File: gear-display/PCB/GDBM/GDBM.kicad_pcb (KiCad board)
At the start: 2 copper layers, 7 parts

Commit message: rikki
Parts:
- added ART1: Artwork_DC_Plug_Polarity, KD_Mechanical:ART_DC_POLARITY, F.Cu at (167.4, 131.6)
- added C1: C_1206_10u_50V, KD_Capacitor:C_1206_3216Metric, B.Cu at (150.5, 130.5)
- added C10: C_0603_33p_NP0_5%_100V, KD_Capacitor:C_0603_1608Metric, B.Cu at (134.9, 119.5)
- added C11: C_0805_1u_X7R_25V, KD_Capacitor:C_0805_2012Metric, B.Cu at (139.1, 108.7)
- added C12: C_1206_10u_50V, KD_Capacitor:C_1206_3216Metric, B.Cu at (158.0, 93.5)
- added C13: C_0603_100n_X7R_100V, KD_Capacitor:C_0603_1608Metric, B.Cu at (156.0, 94.2)
- added C14: C_0603_100n_X7R_100V, KD_Capacitor:C_0603_1608Metric, B.Cu at (104.0, 145.5)
- added C15: C_0805_DNP, KD_Capacitor:C_0805_2012Metric_DNP, B.Cu at (107.5, 145.5)
- added C16: C_1206_10u_50V, KD_Capacitor:C_1206_3216Metric, B.Cu at (95.7, 99.0)
- added C17: C_1206_10u_50V, KD_Capacitor:C_1206_3216Metric, B.Cu at (93.3, 99.0)
- added C18: C_1206_10u_50V, KD_Capacitor:C_1206_3216Metric, B.Cu at (95.7, 94.3)
- added C19: C_0603_100n_X7R_100V, KD_Capacitor:C_0603_1608Metric, B.Cu at (107.4, 122.8)
- added C2: C_1206_10u_50V, KD_Capacitor:C_1206_3216Metric, B.Cu at (154.0, 145.5)
- added C20: C_0805_DNP, KD_Capacitor:C_0805_2012Metric_DNP, B.Cu at (110.0, 123.0)
- added C21: C_0805_1u_X7R_25V, KD_Capacitor:C_0805_2012Metric, B.Cu at (130.6, 95.5)
- added C3: C_1206_10u_50V, KD_Capacitor:C_1206_3216Metric, B.Cu at (148.0, 130.5)
- added C4: C_0603_100n_X7R_100V, KD_Capacitor:C_0603_1608Metric, B.Cu at (156.5, 146.0)
- added C5: C_0603_100n_X7R_100V, KD_Capacitor:C_0603_1608Metric, B.Cu at (145.5, 131.2)
- added C6: C_0603_100n_X7R_100V, KD_Capacitor:C_0603_1608Metric, B.Cu at (116.0, 112.0)
- added C7: C_0805_1u_X7R_25V, KD_Capacitor:C_0805_2012Metric, B.Cu at (118.0, 112.0)
- added C8: C_0603_33p_NP0_5%_100V, KD_Capacitor:C_0603_1608Metric, B.Cu at (126.7, 119.5)
- added C9: C_0805_1u_X7R_25V, KD_Capacitor:C_0805_2012Metric, B.Cu at (132.5, 98.0)
- added D1: Schottky_30V_1A_Toshiba_CUS10S30, KD_Diode:D_SOD-323, B.Cu at (157.0, 137.5)
- added D2: TVS_12V_LF_SMAJ12CA, KD_Diode:DIOC530X280X230_SMA_A, B.Cu at (160.0, 141.5)
- added D3: 0603_Green_Clear_LTST-C190KGKT, KD_Diode:LED_0603_1608Metric_Pad1.05x0.95mm_HandSolder, B.Cu at (116.0, 122.1)
- added D4: TVS_5V5_DRTR5V0U4S-7-M, KD_Package_TO_SOT_SMD:SOT-363_SC-70-6, B.Cu at (157.0, 98.7)
- added D5: 7seg_70mm_CA_Lumex_LDS-AD16RI, KD_Display:7seg_70mm_Kingbright_SC23-11SURKWA, F.Cu at (121.0, 113.0)
- added F1: Fuse_1A_C1F_1, KD_Resistor:RESC3216X70N, B.Cu at (162.5, 137.5)
- added FB1: Ferrite_250mA_Murata_BLM15HG102SN1D, KD_Inductor:INDC1005X55N, B.Cu at (161.0, 98.7)
- added H3: NPTH_3.2_M3_Clearance, KD_Mechanical_Mounting_Hole:NPTH_3.2mm_M3_clearance, F.Cu at (87.0, 74.0)
- added H4: NPTH_3.2_M3_Clearance, KD_Mechanical_Mounting_Hole:NPTH_3.2mm_M3_clearance, F.Cu at (175.0, 153.0)
- added H5: NPTH_3.2_M3_Clearance, KD_Mechanical_Mounting_Hole:NPTH_3.2mm_M3_clearance, F.Cu at (175.0, 74.0)
- added H6: NPTH_3.2_M3_Clearance, KD_Mechanical_Mounting_Hole:NPTH_3.2mm_M3_clearance, F.Cu at (155.0, 119.0)
- added J1: Con_Screw_1x04_691313510004, KD_Connector_Screw:CON_508_1X04_691313510004_Mated, F.Cu at (88.0, 113.5)
- added J2: Con_Screw_1x04_691313510004, KD_Connector_Screw:CON_508_1X04_691313510004_Mated, F.Cu at (174.0, 90.0)
- added J3: DC_2.5_5.5_PJ-090BH, KD_Connector_Circular:CON_DC_2.5_5.5_PJ-090BH, B.Cu at (159.8, 128.0)
- added J4: Con_Screw_1x04_691313510004, KD_Connector_Screw:CON_508_1X04_691313510004_Mated, F.Cu at (88.0, 90.0)
- added J5: Con_Screw_1x04_691313510004, KD_Connector_Screw:CON_508_1X04_691313510004_Mated, F.Cu at (174.0, 113.5)
- added J6: Con_Screw_1x04_691313510004, KD_Connector_Screw:CON_508_1X04_691313510004_Mated, F.Cu at (88.0, 137.0)
- added J7: Con_Screw_1x04_691313510004, KD_Connector_Screw:CON_508_1X04_691313510004_Mated, F.Cu at (174.0, 137.0)
- added J8: USB_B_V_Adam_USB-B-S-VT, KD_Connector_USB_HDMI_Etc:USB_B_Vertical_Adam_USB-B-S-VT, B.Cu at (162.0, 106.0)
- added M1: Knob_6mm_BL_RED_CLIFF_CL170842CR, KD_Mechanical:Knob_CLIFF_CL170842CR, F.Cu at (160.5, 81.5)
- added Q1: PMOS_30V_4A1_SIL3407-TP, KD_Package_TO_SOT_SMD:SOT95P280X120-6RN, B.Cu at (110.0, 141.0)
- added R1: R_0805_DNP, KD_Resistor:RESC2012X60N_DNP, B.Cu at (130.9, 118.5)
- added R10: R_0603_10_5%, KD_Resistor:RESC1608X55N, B.Cu at (152.8, 97.7)
- added R11: R_1206_191_1%, KD_Resistor:RESC3216X70N, B.Cu at (122.5, 89.5)
- added R12: R_1206_191_1%, KD_Resistor:RESC3216X70N, B.Cu at (124.5, 137.5)
- added R13: R_1206_191_1%, KD_Resistor:RESC3216X70N, B.Cu at (116.5, 137.5)
- added R14: R_1206_191_1%, KD_Resistor:RESC3216X70N, B.Cu at (110.5, 89.5)
- added R15: R_0603_22k_1%, KD_Resistor:RESC1608X55N, B.Cu at (99.0, 141.0)
- added R16: R_1206_191_1%, KD_Resistor:RESC3216X70N, B.Cu at (126.5, 89.5)
- added R17: R_1206_191_1%, KD_Resistor:RESC3216X70N, B.Cu at (120.5, 137.5)
- added R18: R_1206_191_1%, KD_Resistor:RESC3216X70N, B.Cu at (114.5, 89.5)
- added R19: R_1206_191_1%, KD_Resistor:RESC3216X70N, B.Cu at (118.5, 89.5)
- added R2: R_0603_22k_1%, KD_Resistor:RESC1608X55N, B.Cu at (135.9, 115.0)
- added R20: R_0805_DNP, KD_Resistor:RESC2012X60N_DNP, B.Cu at (99.0, 93.5)
- added R21: R_0805_0_automotive, KD_Resistor:RESC2012X60N, B.Cu at (92.0, 91.6)
- added R22: R_0805_0_automotive, KD_Resistor:RESC2012X60N, B.Cu at (99.0, 95.5)
- added R23: R_0805_0_automotive, KD_Resistor:RESC2012X60N, B.Cu at (162.9, 121.0)
- added R24: R_0805_0_automotive, KD_Resistor:RESC2012X60N, B.Cu at (162.9, 119.0)
- added R25: R_0805_0_automotive, KD_Resistor:RESC2012X60N, B.Cu at (162.9, 117.0)
- added R26: R_0603_22k_1%, KD_Resistor:RESC1608X55N, B.Cu at (102.0, 123.5)
- added R27: R_0603_22k_1%, KD_Resistor:RESC1608X55N, B.Cu at (100.0, 123.5)
- added R28: Pot_V_10k_CUI_PT01-D120K2-B103, KD_Resistor:Potentiometer_CUI_PT01-DX20K2-XXXX, F.Cu at (160.5, 88.8)
- added R29: R_0402_4700_1%, KD_Resistor:RESC1005X40N, B.Cu at (130.0, 92.5)
- added R3: R_0603_360_1%, KD_Resistor:RESC1608X55N, B.Cu at (116.0, 118.8)
- added R30: R_0603_DNP, KD_Resistor:RESC1608X55N_DNP, B.Cu at (97.1, 141.0)
- added R31: R_0402_4700_1%, KD_Resistor:RESC1005X40N, B.Cu at (92.0, 141.7)
- added R32: R_0402_4700_1%, KD_Resistor:RESC1005X40N, B.Cu at (93.6, 141.7)
- added R4: R_0603_22k_1%, KD_Resistor:RESC1608X55N, B.Cu at (117.0, 104.0)
- added R5: R_0603_DNP, KD_Resistor:RESC1608X55N_DNP, B.Cu at (121.0, 119.0)
- added R6: R_0603_360_1%, KD_Resistor:RESC1608X55N, B.Cu at (121.0, 122.0)
- added R7: R_0603_360_1%, KD_Resistor:RESC1608X55N, B.Cu at (119.0, 122.0)
- added R8: R_0402_DNP, KD_Resistor:RESC1005X40N, B.Cu at (137.9, 116.0)
- added R9: R_0603_10_5%, KD_Resistor:RESC1608X55N, B.Cu at (152.8, 99.7)
- added U1: DC_DC_5V_0A5_K78U05-500R3, KD_IC_DCDC_Converter:DC_DC_Mornsun_K78U05-500R3_H, B.Cu at (150.5, 141.5)
- added U2: ATmega32U4-AU, KD_Package_QFP:QFP80P1200X1200X120-44R_N, B.Cu at (128.9, 108.0)
- added U3: Gate_Driver_MCP1401T-E-OT, KD_Package_TO_SOT_SMD:SOT95P280X145-5N, B.Cu at (104.0, 141.0)
- added U4: Shift_register_OC_8bit_STPIC6D595MTR, KD_Package_SO:SOIC127P640X200-16N, B.Cu at (106.0, 114.0)
- added X1: Programming_AVR_ISP_Staggered_Holes, KD_Connector_Pads:CON_PINHD_1X06_TH_OFFSET, B.Cu at (142.8, 111.3)
- added X2: CON_1x04_TH_staggered, KD_Connector_Pads:CON_PINHD_1X04_TH_OFFSET, B.Cu at (120.7, 129.0)
- added Y1: Crystal_16M_AS-16.000-18-SMD-TR, KD_Oscillator:OSC_CRYSTAL_HC49_US_N, B.Cu at (131.9, 123.5)
- FD1, FD5, FD6: moved to B.Cu
- H1: value M2_NPTH_2.2_Minimal -> NPTH_3.2_M3_Clearance; footprint KD_Mechanical_Mounting_Hole:MountingHole_2.2mm_NPTH -> KD_Mechanical_Mounting_Hole:NPTH_3.2mm_M3_clearance
- moved FD2 130.5 mm to (170.0, 76.0)
- moved FD6 125.3 mm to (171.0, 75.0), turned to 180 degrees
- moved FD3 114.7 mm to (171.0, 151.0)
- moved FD1 112.9 mm to (171.8, 149.8), turned to 180 degrees
- moved H1 37.2 mm to (87.0, 153.0)
- moved FD4 35.2 mm to (89.4, 149.3)
- moved FD5 32.5 mm to (91.0, 150.0), turned to 180 degrees
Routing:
- net +5V: track 0.00 -> 243.4 mm, vias 0 -> 3
- net /7-Segment Display/PWM: track 0.00 -> 152.9 mm, vias 0 -> 4
- net /7-Segment Display/12V_PWM: track 0.00 -> 79.2 mm
- net /MCU/D0(RX): track 0.00 -> 76.8 mm, vias 0 -> 1
- net /MCU/D1(TX): track 0.00 -> 76.4 mm, vias 0 -> 2
- net /MCU/D4: track 0.00 -> 70.3 mm, vias 0 -> 1
- net /MCU/D12: track 0.00 -> 65.7 mm, vias 0 -> 2
- net /MCU/D9: track 0.00 -> 62.1 mm, vias 0 -> 2
- net /MCU/A0(D18): track 0.00 -> 57.2 mm
- net /MCU/D8: track 0.00 -> 56.8 mm, vias 0 -> 2
- net /Interfaces/SDA: track 0.00 -> 56.4 mm, vias 0 -> 4
- net /Interfaces/SCL: track 0.00 -> 54.8 mm, vias 0 -> 2
- net /MCU/A1(D19): track 0.00 -> 54.0 mm
- net /MCU/A2(D20): track 0.00 -> 50.1 mm
- net /7-Segment Display/c: track 0.00 -> 49.9 mm, vias 0 -> 2
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- added copper zone on B.Cu, net +12V
- added copper zone on F.Cu, net +12V
- added copper zone on B.Cu, net /7-Segment Display/12V_PWM
- added copper zone on B.Cu, net GND
- added copper zone on F.Cu, net GND
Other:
- board outline added: 96 x 87 mm
- board text added: "1 2 3 4"
- board text added: "12 V"
- board text added: "Clearance for display"
- board text added: "Teemu Latonen | KD Oy | 000065 Rev 1.0"

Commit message: maybe ok
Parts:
- added X3: CON_GND_Probe_Hook, KD_Connector_Pads:GND_HOOK_M, B.Cu at (163.5, 154.1)
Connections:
- net GND renamed Earth

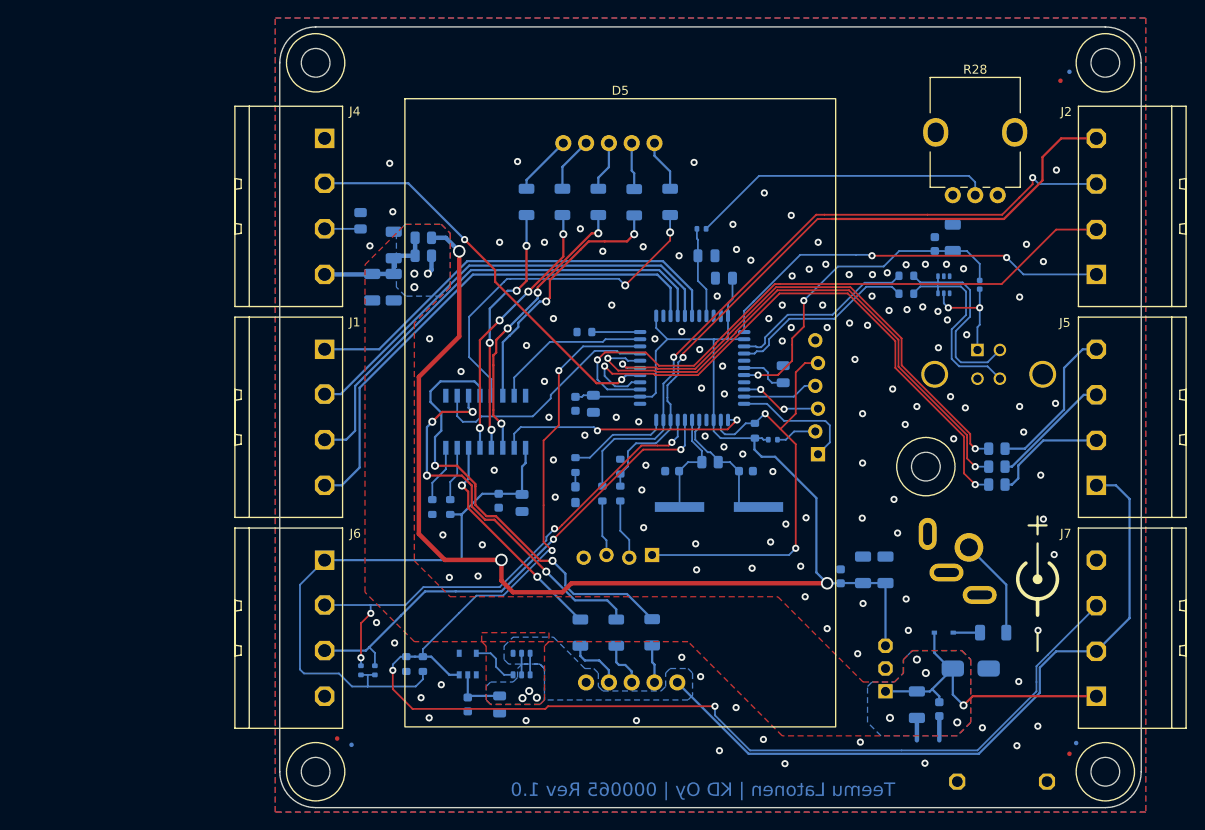
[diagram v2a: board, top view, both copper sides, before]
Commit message: PSU and LED powering changed
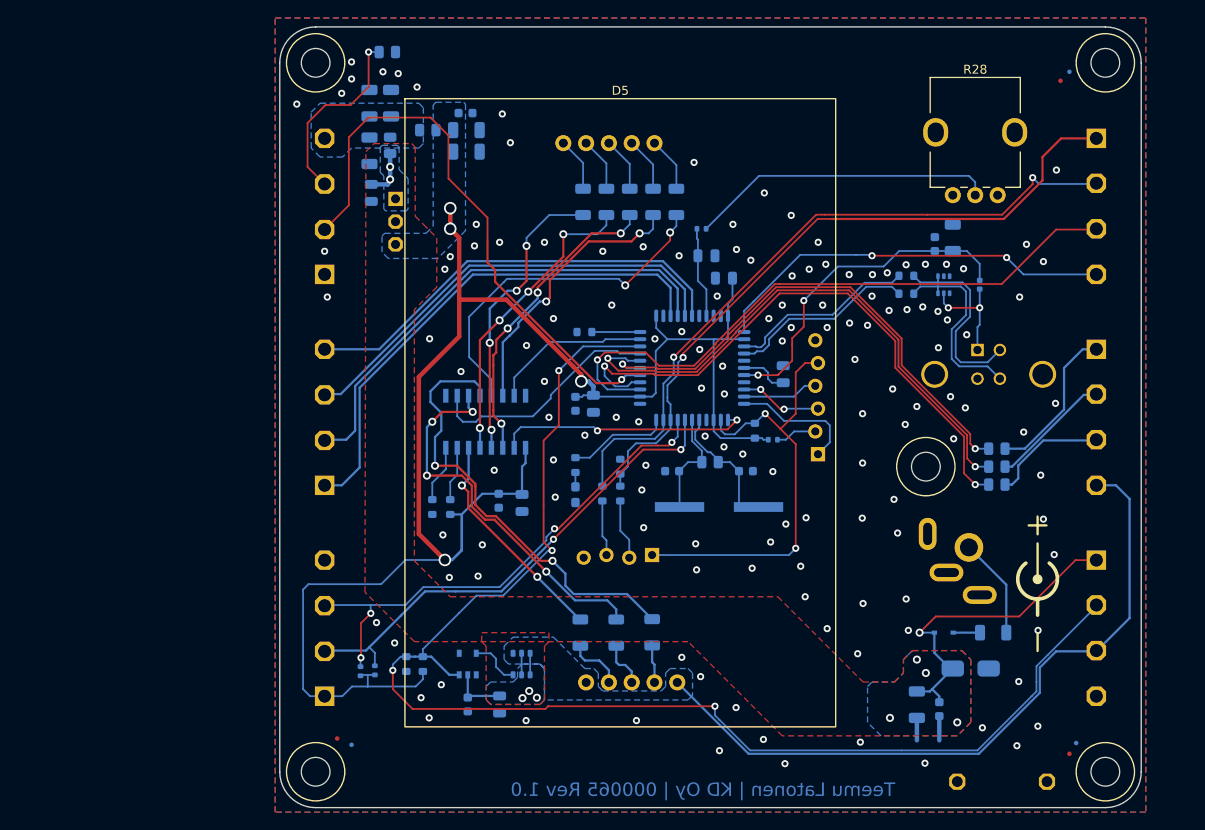
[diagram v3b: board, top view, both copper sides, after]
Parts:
- added C22: C_0805_22u_X5R_10V, KD_Capacitor:CAPC2012X135N, B.Cu at (93.2, 88.5)
- C1, C12, C16, C17, C18, C2, C3: footprint KD_Capacitor:C_1206_3216Metric -> KD_Capacitor:CAPC3216X150N
- C10, C13, C14, C19, C4, C5, C6, C8: footprint KD_Capacitor:C_0603_1608Metric -> KD_Capacitor:CAPC1608X90N
- C11, C21, C7, C9: footprint KD_Capacitor:C_0805_2012Metric -> KD_Capacitor:CAPC2012X135N
- C15, C20: footprint KD_Capacitor:C_0805_2012Metric_DNP -> KD_Capacitor:CAPC2012X135N_DNP
- J1, J2, J4, J5, J6, J7: moved to B.Cu
- R20: value R_0805_DNP -> R_0805_0_automotive; footprint KD_Resistor:RESC2012X60N_DNP -> KD_Resistor:RESC2012X60N
- R22: value R_0805_0_automotive -> R_0805_DNP; footprint KD_Resistor:RESC2012X60N -> KD_Resistor:RESC2012X60N_DNP
- U1: footprint KD_IC_DCDC_Converter:DC_DC_Mornsun_K78U05-500R3_H -> KD_IC_DCDC_Converter:DC_DC_GAPTEC_OKI-78SR-5_H
- moved U1 73.9 mm to (95.9, 91.7), turned to 90 degrees
- moved C5 66.4 mm to (103.7, 79.6), turned to 0 degrees
- moved C3 66.0 mm to (103.8, 81.5), turned to 0 degrees
- moved C1 66.0 mm to (103.8, 83.9), turned to 0 degrees
- moved C17 20.6 mm to (95.4, 78.5), turned to 90 degrees
- moved R21 19.0 mm to (95.0, 72.8), turned to 0 degrees
- moved C18 16.0 mm to (93.0, 78.5)
- moved C16 15.4 mm to (93.0, 83.8)
- moved R22 12.8 mm to (95.3, 83.2), turned to 90 degrees
- moved R20 12.0 mm to (99.5, 81.5)
- moved R14 6.30 mm to (116.8, 89.5)
- moved R18 4.90 mm to (119.4, 89.5)
- moved R19 3.50 mm to (122.0, 89.5)
- moved R11 2.10 mm to (124.6, 89.5)
- moved R32 1.60 mm to (92.0, 141.8)
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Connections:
- net Net-(C16-Pad1) renamed /RPM Bar/LED_PWR
- J1 pad 1: /MCU/A3(D21) -> /MCU/A0(D18)
- J1 pad 2: /MCU/A2(D20) -> /MCU/A1(D19)
- J1 pad 3: /MCU/A1(D19) -> /MCU/A2(D20)
- J1 pad 4: /MCU/A0(D18) -> /MCU/A3(D21)
- J2 pad 1: /MCU/D7 -> /MCU/D0(RX)
- J2 pad 2: /MCU/D4 -> /MCU/D1(TX)
- J2 pad 3: /MCU/D1(TX) -> /MCU/D4
- J2 pad 4: /MCU/D0(RX) -> /MCU/D7
- J5 pad 1: /7-Segment Display/12V_PWM -> Net-(R25-Pad1)
- J5 pad 2: Net-(J5-Pad2) -> Net-(R24-Pad1)
- J5 pad 3: Net-(J5-Pad3) -> Net-(R23-Pad1)
- J5 pad 4: Net-(J5-Pad4) -> /7-Segment Display/12V_PWM
- J6 pad 2: /Interfaces/SDA -> /Interfaces/SCL
- J6 pad 3: /Interfaces/SCL -> /Interfaces/SDA
- J7 pad 2: /7-Segment Display/12V_PWM -> /7-Segment Display/PWM
- J7 pad 3: /7-Segment Display/PWM -> /7-Segment Display/12V_PWM
- R23 pad 1: Net-(J5-Pad2) -> Net-(R23-Pad1)
- R24 pad 1: Net-(J5-Pad3) -> Net-(R24-Pad1)
- R25 pad 1: Net-(J5-Pad4) -> Net-(R25-Pad1)
- R31 pad 2: /Interfaces/SDA -> /Interfaces/SCL
- R32 pad 2: /Interfaces/SCL -> /Interfaces/SDA
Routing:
- net +5V: track 243.4 -> 181.6 mm, vias 3 -> 4
- net /MCU/D6: track 45.5 -> 63.9 mm, vias 2 -> 1
- net Net-(R25-Pad1): track 0.00 -> 17.5 mm
- net Net-(J5-Pad4): track 17.5 -> 0.00 mm
- net /RPM Bar/LED_STRIP_B: track 4.01 -> 21.1 mm, vias 0 -> 1
- net /RPM Bar/LED_PWR: track 14.0 -> 0.00 mm
- net Net-(R24-Pad1): track 0.00 -> 13.5 mm
- net Net-(J5-Pad3): track 13.5 -> 0.00 mm
- net Net-(R23-Pad1): track 0.00 -> 13.1 mm
- net Net-(J5-Pad2): track 13.1 -> 0.00 mm
- net /7-Segment Display/g: track 28.1 -> 32.9 mm
- net /7-Segment Display/f: track 29.6 -> 33.8 mm
- net +12V: track 48.3 -> 52.3 mm, vias 11 -> 10
- net /7-Segment Display/dp: track 31.5 -> 34.4 mm
- net /7-Segment Display/a: track 29.3 -> 31.1 mm
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- added copper zone on B.Cu, net +5V
- added copper zone on B.Cu, net /RPM Bar/LED_PWR
